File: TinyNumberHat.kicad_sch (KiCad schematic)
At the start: 32 parts, among them IC1 SamacSys_Parts_HT16K33-28SOP, J1 GPIO, J3 SM04B-SRSS-TB(LF)(SN), SW1 SW_Omron_B3FS, SW2 SW_Omron_B3FS, SW3 SW_Omron_B3FS, SW4 SW_Omron_B3FS

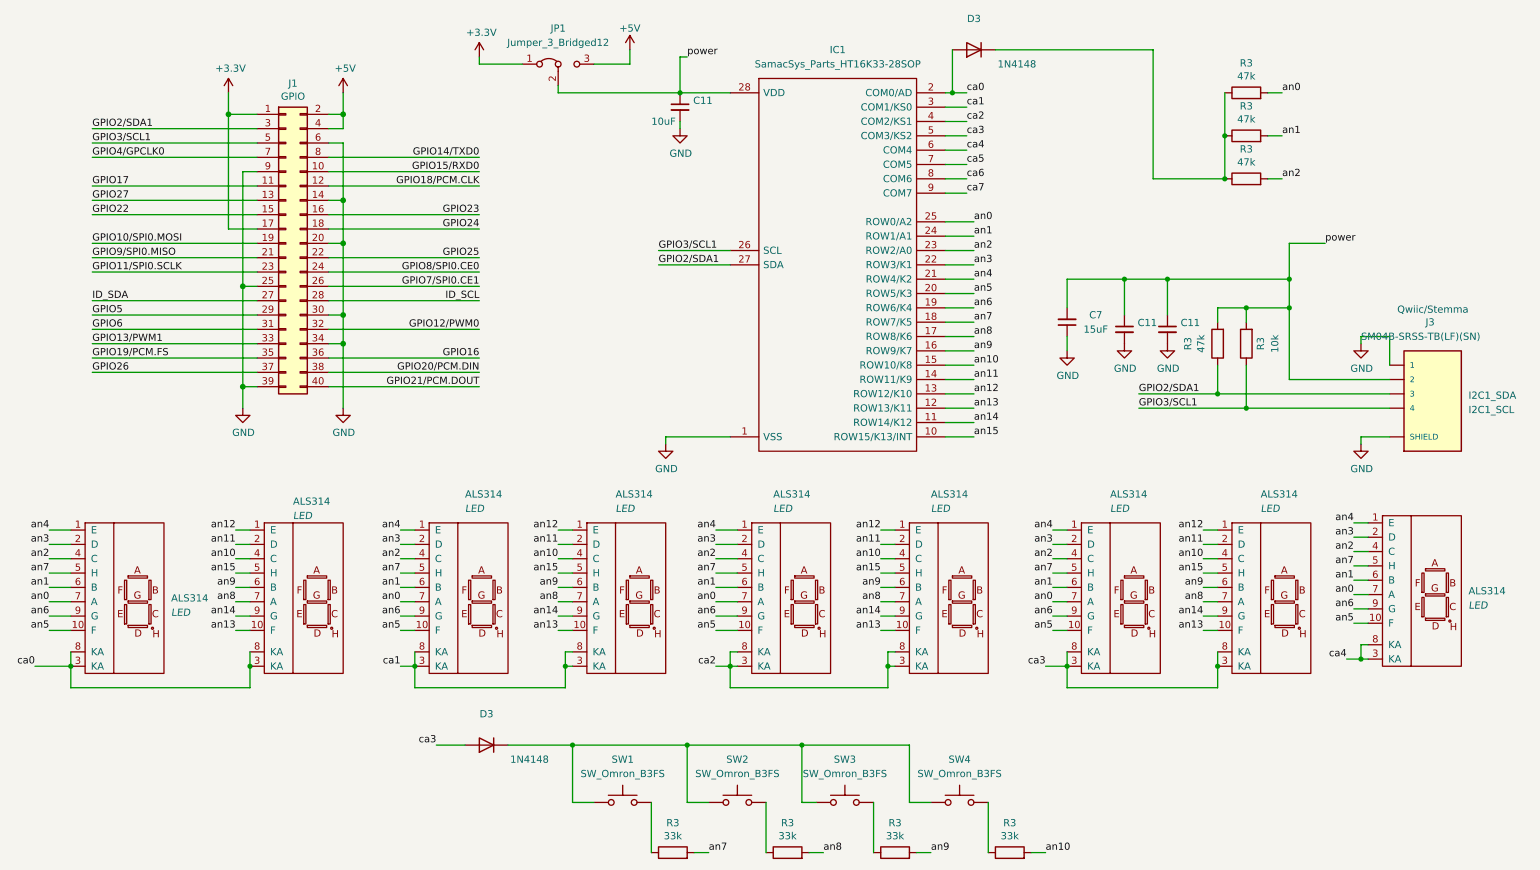
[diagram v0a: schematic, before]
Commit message: Update silkscreens
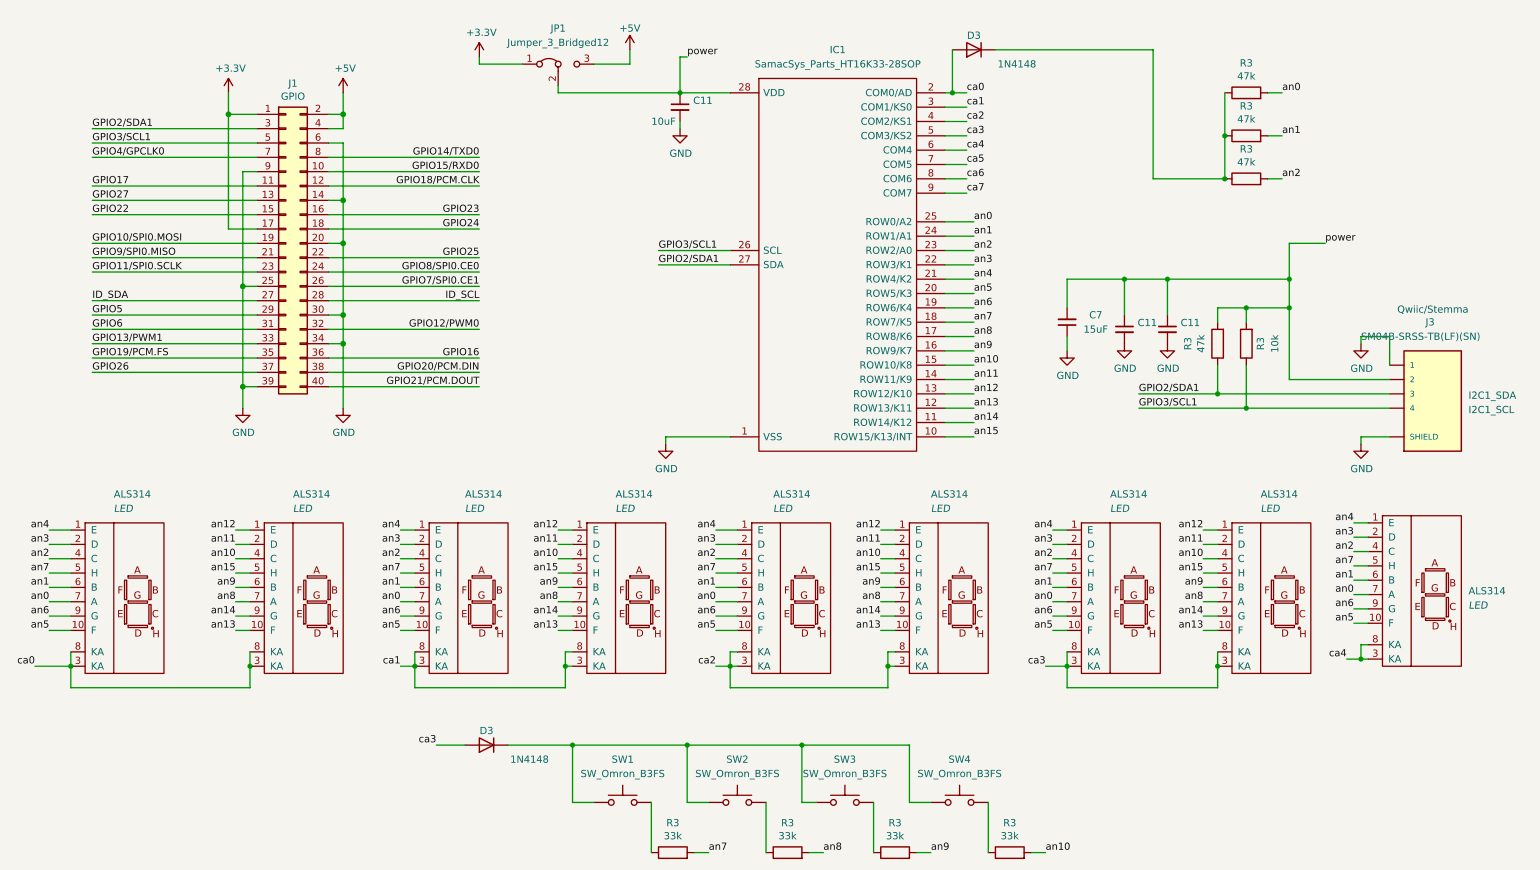
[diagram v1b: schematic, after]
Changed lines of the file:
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@@
   (symbol (lib_id "Device:D") (at 101.6 139.7 180) (unit 1)
     (in_bom yes) (on_board yes) (dnp no)
-    (property "Reference" "D3" (at 101.6 134.1882 0)
+    (property "Reference" "D3" (at 101.6 137.16 0)
       (effects (font (size 1.27 1.27)))
     )
@@
       (effects (font (size 1.27 1.27) italic) (justify left) hide)
     )
-    (property "Value" "ALS314" (at 67.31 96.52 0)
+    (property "Value" "ALS314" (at 67.31 95.25 0)
       (effects (font (size 1.27 1.27)) (justify left))
     )
@@
       (effects (font (size 1.27 1.27)) hide)
     )
-    (property "Тип" "LED" (at 67.31 99.06 0)
+    (property "Тип" "LED" (at 67.31 97.79 0)
       (effects (font (size 1.27 1.27) italic) (justify left))
     )
@@
   (symbol (lib_id "Device:D") (at 187.96 16.51 180) (unit 1)
     (in_bom yes) (on_board yes) (dnp no)
-    (property "Reference" "D3" (at 187.96 10.9982 0)
+    (property "Reference" "D3" (at 187.96 13.97 0)
       (effects (font (size 1.27 1.27)))
     )
@@
   )
   (symbol (lib_id "LTP-305G:АЛС314") (at 27.94 101.6 0) (unit 1)
-    (in_bom yes) (on_board yes) (dnp no) (fields_autoplaced)
+    (in_bom yes) (on_board yes) (dnp no)
     (property "Reference" "DPY1" (at 45.72 111.125 0)
       (effects (font (size 1.27 1.27) italic) (justify left) hide)
     )
-    (property "Value" "ALS314" (at 45.72 113.665 0)
+    (property "Value" "ALS314" (at 35.56 95.25 0)
       (effects (font (size 1.27 1.27)) (justify left))
     )
@@
       (effects (font (size 1.27 1.27)) hide)
     )
-    (property "Тип" "LED" (at 45.72 116.205 0)
+    (property "Тип" "LED" (at 35.56 97.79 0)
       (effects (font (size 1.27 1.27) italic) (justify left))
     )
